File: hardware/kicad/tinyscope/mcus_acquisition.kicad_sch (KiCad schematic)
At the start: 30 parts, among them J5 STM32H743, Q2 NMOS, SW1 SW_SPST, U12 STM32H743VITx, X1 25MHz, X2 32k768

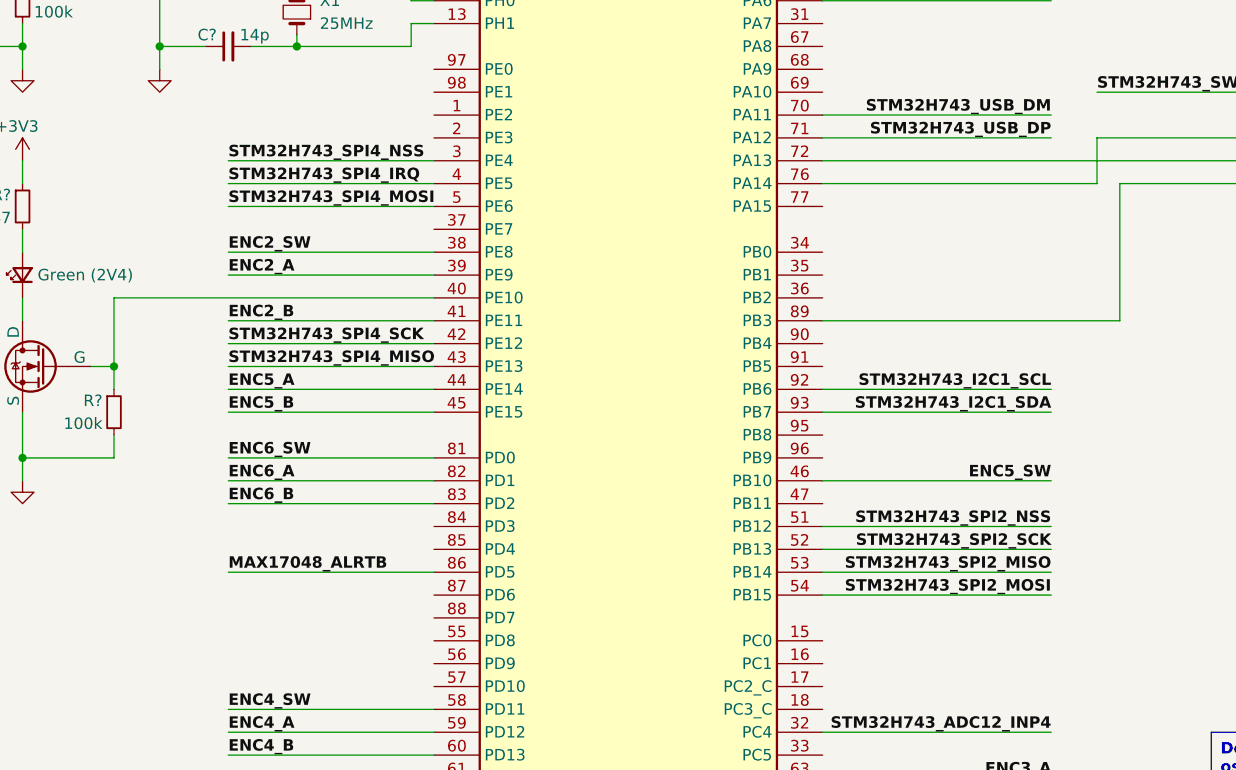
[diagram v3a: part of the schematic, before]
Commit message: fix: hardware: Solves electrical rules warnings and errors #6
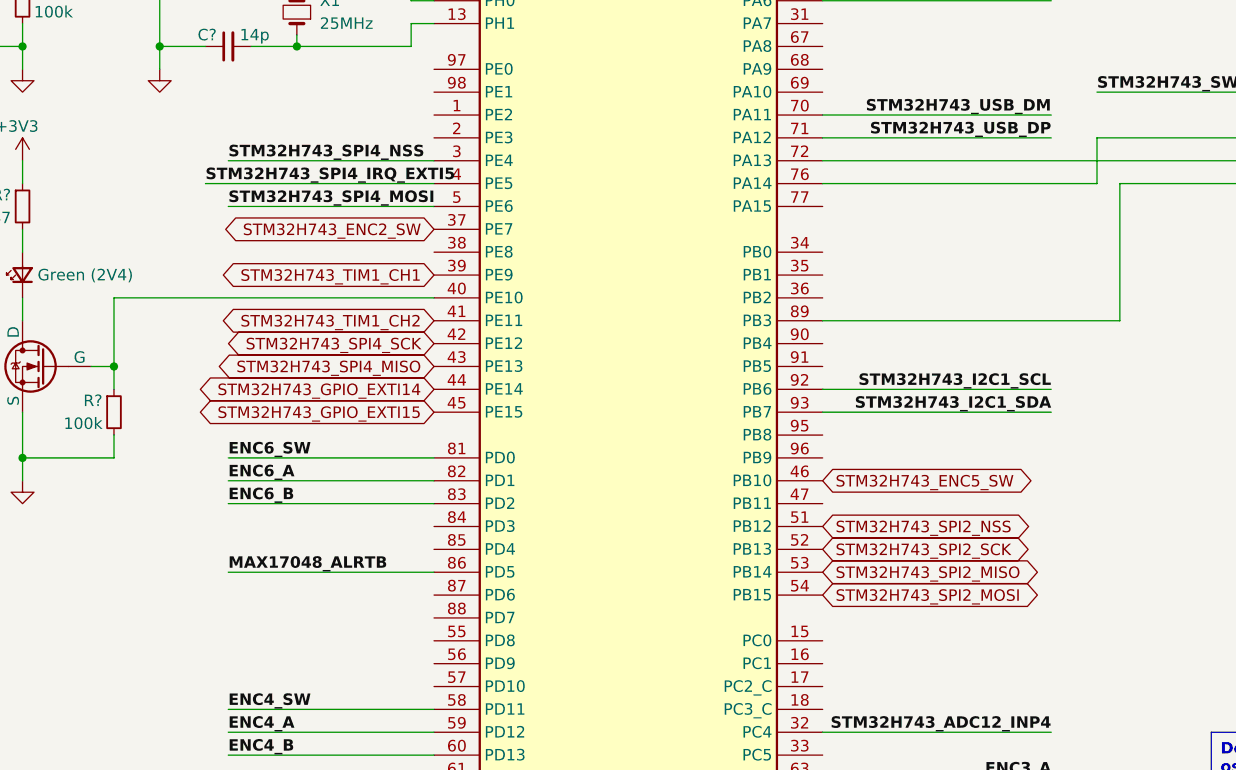
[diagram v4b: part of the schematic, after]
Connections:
- net STM32H743_ENC2_SW: now reaches U12.37 (PE7)
- net ENC2_A renamed STM32H743_TIM1_CH1
- net ENC2_B renamed STM32H743_TIM1_CH2
- net ENC2_SW: no longer names the net of U12.38 (PE8)
- net ENC5_A renamed STM32H743_GPIO_EXTI14
- net ENC5_B renamed STM32H743_GPIO_EXTI15
- net ENC5_SW renamed STM32H743_ENC5_SW
- net STM32H743_SPI4_IRQ renamed STM32H743_SPI4_IRQ_EXTI5
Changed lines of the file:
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@@
-    (stroke (width 0) (type default))
-  )
-  (wire (pts (xy 177.8 109.22) (xy 203.2 109.22))
     (stroke (width 0) (type default))
   )
@@
     (stroke (width 0) (type default))
   )
-  (wire (pts (xy 134.62 78.74) (xy 111.76 78.74))
-    (stroke (width 0) (type default))
-  )
-  (wire (pts (xy 177.8 114.3) (xy 203.2 114.3))
-    (stroke (width 0) (type default))
-  )
   (wire (pts (xy 198.12 149.86) (xy 198.12 152.4))
     (stroke (width 0) (type default))
@@
     (stroke (width 0) (type default))
   )
-  (wire (pts (xy 111.76 71.12) (xy 134.62 71.12))
-    (stroke (width 0) (type default))
-  )
-  (wire (pts (xy 111.76 91.44) (xy 134.62 91.44))
+  (wire (pts (xy 109.22 71.12) (xy 134.62 71.12))
     (stroke (width 0) (type default))
   )
@@
     (stroke (width 0) (type default))
   )
-  (wire (pts (xy 134.62 96.52) (xy 111.76 96.52))
-    (stroke (width 0) (type default))
-  )
-  (wire (pts (xy 134.62 86.36) (xy 111.76 86.36))
-    (stroke (width 0) (type default))
-  )
   (wire (pts (xy 73.66 30.48) (xy 73.66 27.94))
     (stroke (width 0) (type default))
@@
     (stroke (width 0) (type default))
   )
-  (wire (pts (xy 177.8 111.76) (xy 203.2 111.76))
-    (stroke (width 0) (type default))
-  )
   (wire (pts (xy 208.28 66.04) (xy 208.28 71.12))
     (stroke (width 0) (type default))
   )
-  (wire (pts (xy 177.8 104.14) (xy 203.2 104.14))
-    (stroke (width 0) (type default))
-  )
   (wire (pts (xy 134.62 104.14) (xy 111.76 104.14))
     (stroke (width 0) (type default))
@@
     (stroke (width 0) (type default))
   )
-  (wire (pts (xy 134.62 93.98) (xy 111.76 93.98))
-    (stroke (width 0) (type default))
-  )
   (wire (pts (xy 119.38 154.94) (xy 119.38 157.48))
     (stroke (width 0) (type default))
@@
     (stroke (width 0) (type default))
   )
-  (wire (pts (xy 111.76 88.9) (xy 134.62 88.9))
-    (stroke (width 0) (type default))
-  )
   (wire (pts (xy 177.8 35.56) (xy 203.2 35.56))
     (stroke (width 0) (type default))
@@
     (stroke (width 0) (type default))
   )
-  (wire (pts (xy 177.8 116.84) (xy 203.2 116.84))
-    (stroke (width 0) (type default))
-  )
   (wire (pts (xy 156.21 172.72) (xy 156.21 175.26))
     (stroke (width 0) (type default))
@@
   )
   (wire (pts (xy 208.28 71.12) (xy 177.8 71.12))
-    (stroke (width 0) (type default))
-  )
-  (wire (pts (xy 134.62 81.28) (xy 111.76 81.28))
     (stroke (width 0) (type default))
   )
@@
     (effects (font (size 1.27 1.27) bold) (justify left bottom))
   )
-  (label "STM32H743_SPI2_NSS" (at 203.2 109.22 180) (fields_autoplaced)
-    (effects (font (size 1.27 1.27) bold) (justify right bottom))
-  )
-  (label "ENC2_SW" (at 111.76 78.74 0) (fields_autoplaced)
-    (effects (font (size 1.27 1.27) bold) (justify left bottom))
-  )
-  (label "STM32H743_SPI2_SCK" (at 203.2 111.76 180) (fields_autoplaced)
-    (effects (font (size 1.27 1.27) bold) (justify right bottom))
-  )
   (label "STM32H743_USB_DP" (at 203.2 66.04 180) (fields_autoplaced)
     (effects (font (size 1.27 1.27) bold) (justify right bottom))
@@
     (effects (font (size 1.27 1.27) bold) (justify right bottom))
   )
-  (label "STM32H743_SPI4_SCK" (at 111.76 88.9 0) (fields_autoplaced)
-    (effects (font (size 1.27 1.27) bold) (justify left bottom))
-  )
   (label "STM32H743_SWD_NRST" (at 208.28 60.96 0) (fields_autoplaced)
     (effects (font (size 1.27 1.27) bold) (justify left bottom))
@@
     (effects (font (size 1.27 1.27) bold) (justify right bottom))
   )
-  (label "ENC5_SW" (at 203.2 104.14 180) (fields_autoplaced)
-    (effects (font (size 1.27 1.27) bold) (justify right bottom))
-  )
   (label "STM32H743_I2C1_SDA" (at 203.2 96.52 180) (fields_autoplaced)
     (effects (font (size 1.27 1.27) bold) (justify right bottom))
@@
     (effects (font (size 1.27 1.27) bold) (justify right bottom))
   )
-  (label "STM32H743_SPI2_MISO" (at 203.2 114.3 180) (fields_autoplaced)
-    (effects (font (size 1.27 1.27) bold) (justify right bottom))
-  )
   (label "ENC4_B" (at 111.76 134.62 0) (fields_autoplaced)
     (effects (font (size 1.27 1.27) bold) (justify left bottom))
   )
-  (label "STM32H743_SPI2_MOSI" (at 203.2 116.84 180) (fields_autoplaced)
-    (effects (font (size 1.27 1.27) bold) (justify right bottom))
-  )
-  (label "STM32H743_SPI4_MISO" (at 111.76 91.44 0) (fields_autoplaced)
-    (effects (font (size 1.27 1.27) bold) (justify left bottom))
-  )
   (label "ENC4_SW" (at 111.76 129.54 0) (fields_autoplaced)
     (effects (font (size 1.27 1.27) bold) (justify left bottom))
@@
     (effects (font (size 1.27 1.27) bold) (justify left bottom))
   )
-  (label "ENC5_B" (at 111.76 96.52 0) (fields_autoplaced)
-    (effects (font (size 1.27 1.27) bold) (justify left bottom))
-  )
   (label "STM32H743_ADC12_INP4" (at 203.2 132.08 180) (fields_autoplaced)
     (effects (font (size 1.27 1.27) bold) (justify right bottom))
@@
     (effects (font (size 1.27 1.27) bold) (justify right bottom))
   )
-  (label "ENC2_B" (at 111.76 86.36 0) (fields_autoplaced)
-    (effects (font (size 1.27 1.27) bold) (justify left bottom))
-  )
-  (label "STM32H743_SPI4_IRQ" (at 111.76 71.12 0) (fields_autoplaced)
+  (label "STM32H743_SPI4_IRQ_EXTI5" (at 109.22 71.12 0) (fields_autoplaced)
     (effects (font (size 1.27 1.27) bold) (justify left bottom))
   )
@@
     (effects (font (size 1.27 1.27) bold) (justify right bottom))
   )
-  (label "ENC2_A" (at 111.76 81.28 0) (fields_autoplaced)
-    (effects (font (size 1.27 1.27) bold) (justify left bottom))
-  )
   (label "STM32H743_SPI4_MOSI" (at 111.76 73.66 0) (fields_autoplaced)
     (effects (font (size 1.27 1.27) bold) (justify left bottom))
   )
-  (label "ENC5_A" (at 111.76 93.98 0) (fields_autoplaced)
-    (effects (font (size 1.27 1.27) bold) (justify left bottom))
-  )
   (label "STM32H743_SPI4_NSS" (at 111.76 68.58 0) (fields_autoplaced)
     (effects (font (size 1.27 1.27) bold) (justify left bottom))
@@
     (effects (font (size 1.27 1.27) bold) (justify left bottom))
   )
+  (global_label "STM32H743_SPI2_SCK" (shape bidirectional) (at 177.8 111.76 0) (fields_autoplaced)
+    (effects (font (size 1.27 1.27)) (justify left))
+    (property "Intersheetrefs" "${INTERSHEET_REFS}" (at 202.8021 111.76 0)
+      (effects (font (size 1.27 1.27)) (justify left) hide)
+    )
+  )
+  (global_label "STM32H743_SPI2_MOSI" (shape bidirectional) (at 177.8 116.84 0) (fields_autoplaced)
+    (effects (font (size 1.27 1.27)) (justify left))
+    (property "Intersheetrefs" "${INTERSHEET_REFS}" (at 203.6488 116.84 0)
+      (effects (font (size 1.27 1.27)) (justify left) hide)
+    )
+  )
+  (global_label "STM32H743_SPI2_MISO" (shape bidirectional) (at 177.8 114.3 0) (fields_autoplaced)
+    (effects (font (size 1.27 1.27)) (justify left))
+    (property "Intersheetrefs" "${INTERSHEET_REFS}" (at 203.6488 114.3 0)
+      (effects (font (size 1.27 1.27)) (justify left) hide)
+    )
+  )
+  (global_label "STM32H743_GPIO_EXTI14" (shape bidirectional) (at 134.62 93.98 180) (fields_autoplaced)
+    (effects (font (size 1.27 1.27)) (justify right))
+    (property "Intersheetrefs" "${INTERSHEET_REFS}" (at 106.836 93.98 0)
+      (effects (font (size 1.27 1.27)) (justify right) hide)
+    )
+  )
+  (global_label "STM32H743_SPI2_NSS" (shape bidirectional) (at 177.8 109.22 0) (fields_autoplaced)
+    (effects (font (size 1.27 1.27)) (justify left))
+    (property "Intersheetrefs" "${INTERSHEET_REFS}" (at 202.8021 109.22 0)
+      (effects (font (size 1.27 1.27)) (justify left) hide)
+    )
+  )
+  (global_label "STM32H743_GPIO_EXTI15" (shape bidirectional) (at 134.62 96.52 180) (fields_autoplaced)
+    (effects (font (size 1.27 1.27)) (justify right))
+    (property "Intersheetrefs" "${INTERSHEET_REFS}" (at 106.836 96.52 0)
+      (effects (font (size 1.27 1.27)) (justify right) hide)
+    )
+  )
+  (global_label "STM32H743_TIM1_CH2" (shape bidirectional) (at 134.62 86.36 180) (fields_autoplaced)
+    (effects (font (size 1.27 1.27)) (justify right))
+    (property "Intersheetrefs" "${INTERSHEET_REFS}" (at 109.6179 86.36 0)
+      (effects (font (size 1.27 1.27)) (justify right) hide)
+    )
+  )
+  (global_label "STM32H743_SPI4_MISO" (shape bidirectional) (at 134.62 91.44 180) (fields_autoplaced)
+    (effects (font (size 1.27 1.27)) (justify right))
+    (property "Intersheetrefs" "${INTERSHEET_REFS}" (at 108.7712 91.44 0)
+      (effects (font (size 1.27 1.27)) (justify right) hide)
+    )
+  )
+  (global_label "STM32H743_SPI4_SCK" (shape bidirectional) (at 134.62 88.9 180) (fields_autoplaced)
+    (effects (font (size 1.27 1.27)) (justify right))
+    (property "Intersheetrefs" "${INTERSHEET_REFS}" (at 109.6179 88.9 0)
+      (effects (font (size 1.27 1.27)) (justify right) hide)
+    )
+  )
+  (global_label "STM32H743_TIM1_CH1" (shape bidirectional) (at 134.62 81.28 180) (fields_autoplaced)
+    (effects (font (size 1.27 1.27)) (justify right))
+    (property "Intersheetrefs" "${INTERSHEET_REFS}" (at 109.6179 81.28 0)
+      (effects (font (size 1.27 1.27)) (justify right) hide)
+    )
+  )
+  (global_label "STM32H743_ENC2_SW" (shape bidirectional) (at 134.62 76.2 180) (fields_autoplaced)
+    (effects (font (size 1.27 1.27)) (justify right))
+    (property "Intersheetrefs" "${INTERSHEET_REFS}" (at 110.0413 76.2 0)
+      (effects (font (size 1.27 1.27)) (justify right) hide)
+    )
+  )
+  (global_label "STM32H743_ENC5_SW" (shape bidirectional) (at 177.8 104.14 0) (fields_autoplaced)
+    (effects (font (size 1.27 1.27)) (justify left))
+    (property "Intersheetrefs" "${INTERSHEET_REFS}" (at 202.3787 104.14 0)
+      (effects (font (size 1.27 1.27)) (justify left) hide)
+    )
+  )
   (symbol (lib_id "Device:C_Small") (at 53.34 25.4 0) (mirror y) (unit 1)

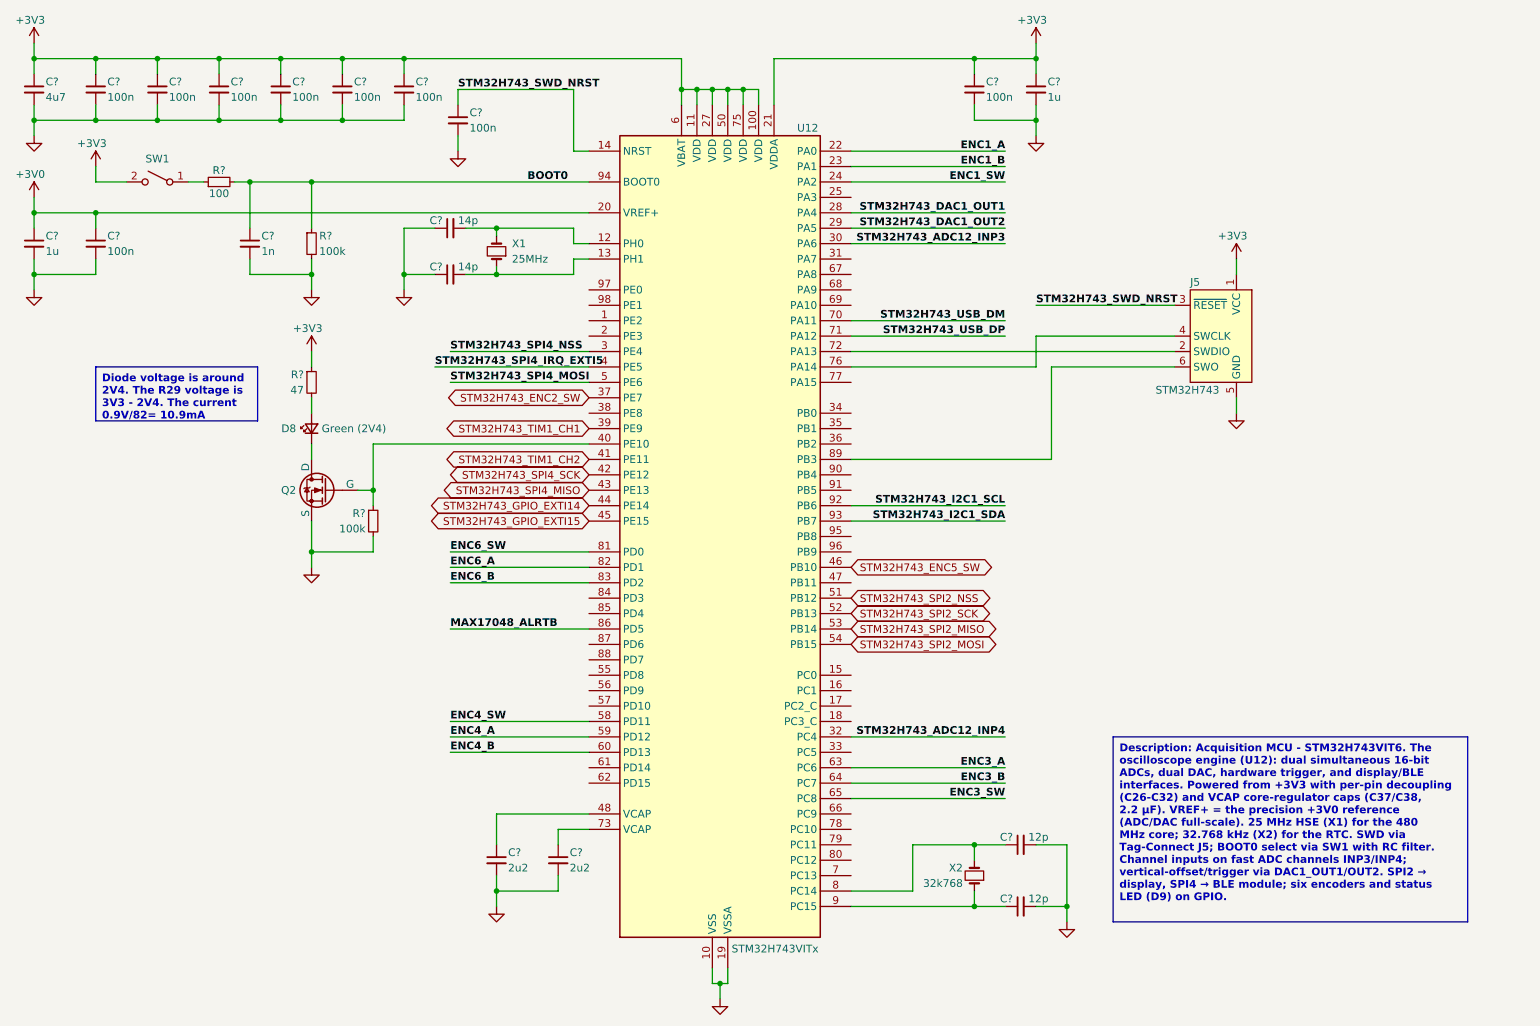
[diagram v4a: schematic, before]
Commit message: feat: hardware: Add global labels for acquisition mcu
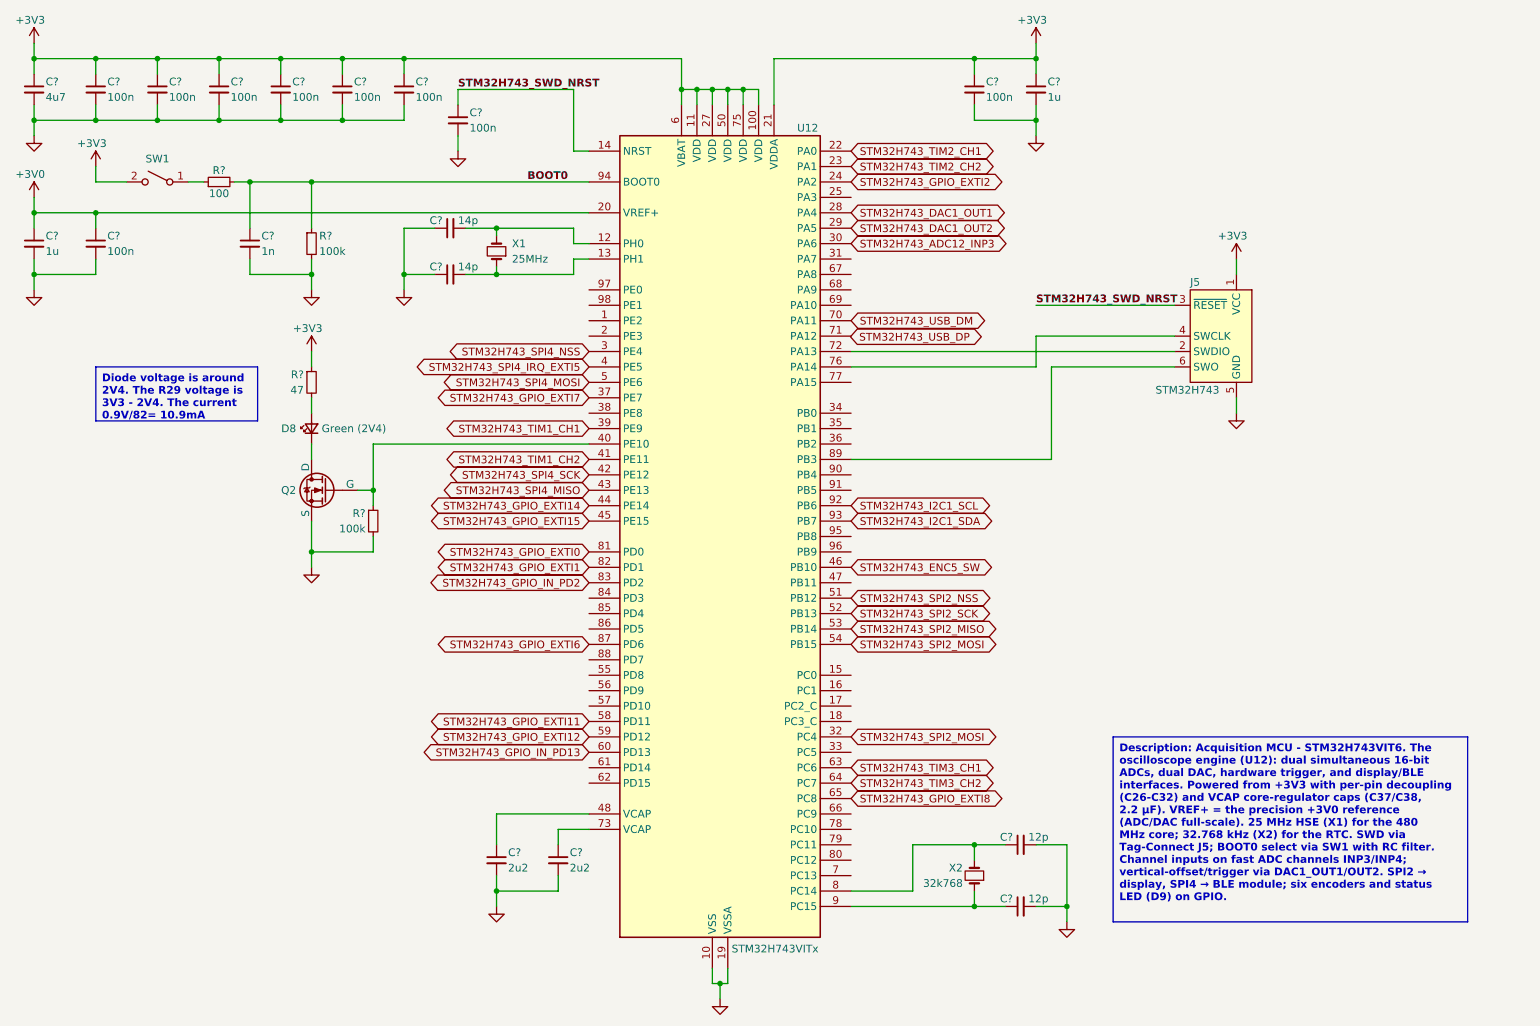
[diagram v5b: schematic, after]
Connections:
- net STM32H743_ADC12_INP4 is gone; now on net STM32H743_SPI2_MOSI: U12.32 (PC4)
- net STM32H743_USB_DP: no longer U12.71 (PA12)
- net STM32H743_GPIO_EXTI6: now reaches U12.87 (PD6)
- net ENC1_A renamed STM32H743_TIM2_CH1
- net ENC1_B renamed STM32H743_TIM2_CH2
- net ENC1_SW renamed STM32H743_GPIO_EXTI2
- net ENC3_A renamed STM32H743_TIM3_CH1
- net ENC3_B renamed STM32H743_TIM3_CH2
- net ENC3_SW renamed STM32H743_GPIO_EXTI8
- net ENC4_A renamed STM32H743_GPIO_EXTI12
- net ENC4_B renamed STM32H743_GPIO_IN_PD13
- net ENC4_SW renamed STM32H743_GPIO_EXTI11
- net ENC6_A renamed STM32H743_GPIO_EXTI1
- net ENC6_B renamed STM32H743_GPIO_IN_PD2
- net ENC6_SW renamed STM32H743_GPIO_EXTI0
- net MAX17048_ALRTB: no longer names the net of U12.86 (PD5)
- net STM32H743_ENC2_SW renamed STM32H743_GPIO_EXTI7
